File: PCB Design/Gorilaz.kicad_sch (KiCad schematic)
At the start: 57 parts, among them J1 Conn_01x13, J2 Conn_01x13, J3 Conn_01x13, J4 Conn_01x13, J5 HRO_TYPE-C-31-M-14, J5 Thermistor, J6 Battery, J6 Thermistor, J7 Conn_01x13, J8 Conn_01x13, J9 Battery, J9 TC2030_SWD, Q2 2N7002, SW1 PWR, SW4 RST, U1 SRV05-4, U10 MAX17048, U3 BQ24075, U4 DW01A, U5 FS8205, U8 nRF52840_moko_mk08

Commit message: LED package
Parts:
- D1, D2, D3, D4: footprint LED_THT:LED_D3.0mm -> LED_SMD:LED_1206_3216Metric
- R1, R2, R3, R4: value R_US -> 10k; footprint Resistor_THT:R_Axial_DIN0204_L3.6mm_D1.6mm_P5.08mm_Horizontal -> Resistor_SMD:R_0805_2012Metric

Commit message: schema update
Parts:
- removed D4: LED_ALT, LED_SMD:LED_1206_3216Metric, symbol kicad_port-rescue:LED_ALT-Device
- removed J5, J6: Thermistor, Connector_JST:JST_PH_S2B-PH-K_1x02_P2.00mm_Horizontal, symbol Connector_Generic_MountingPin:Conn_01x02_MountingPin
- removed J9: Battery, PCM_marbastlib-various:Molex_Pico-EZmate_78171-0002_1x02-1MP_P1.20mm_Vertical, symbol Connector_Generic_MountingPin:Conn_01x02_MountingPin
- removed R14, R16: 5k, Resistor_SMD:R_0402_1005Metric, symbol Device:R_Small
- removed R4: 10k, Resistor_SMD:R_0805_2012Metric, symbol kicad_port-rescue:R_US-Device
- J1, J2, J7, J8: footprint kinesisMod_board_connectors:Molex_0039532135 -> Local:Molex_0039532135
- J3: footprint kinesisMod_board_connectors:Molex_039532134 -> Local:Molex_0039532135
- J4: footprint kinesisMod_board_connectors:Molex_039532134 -> Molex_0039532135
- J6: footprint PCM_marbastlib-various:Molex_Pico-EZmate_78171-0002_1x02-1MP_P1.20mm_Vertical -> Local:Molex_Pico-EZmate_78171-0002_1x02-1MP_P1.20mm_Vertical
- J9: footprint PCM_marbastlib-various:CON_TC2030_outlined -> Local:CON_TC2030_outlined
- SW1: footprint PCM_marbastlib-various:SW_MSK12C02-HB -> Mastarlib:SW_MSK12C02-HB
- SW4: footprint PCM_marbastlib-various:SW_SPST_SKQG_WithStem -> Button_Switch_SMD:SW_SPST_SKQG_WithStem
- U10: footprint Package_DFN_QFN:DFN-8-1EP_2x2mm_P0.5mm_EP0.7x1.3mm -> Local:DFN-8-1EP_2x2mm_P0.5mm_EP0.7x1.3mm
- U8: footprint PCM_marbastlib-various:nRF52840_moko_mk08 -> Mastarlib:nRF52840_moko_mk08
- renumbered R1 to R20, R2 to R21, R3 to R22, R6 to R4, R7 to R6
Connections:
- net UG_EN: no longer names the net of U8.49 (P1.00)
- net UG_LV: no longer names the net of U8.31 (P0.22)
- no-connect marks 31 -> 30
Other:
- note added: "LED2: Battery Charging"
- note removed: "Overtemperature protection (BQ24075) Use a 10k thermistor"
- note removed: "Overtemperature protection (TP4056) For values of R15/R16 as well as the thermistor, refer to the datasheet."
- moved on the sheet: C17, C6, C7, C8, J6, LED2, R10, R15, R17, R18, R19, R9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

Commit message: v0
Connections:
- net LED_CAPS_LOCK: now also U8.13 (P0.04-A); no longer U8.1 (P0.03-LF-A)
- net LED_KEYPAD: now also U8.16 (P0.08); no longer U8.4 (P0.29-LF-A)
- net LED_NUM_LOCK: now also U8.14 (P0.06); no longer U8.2 (P0.02-LF-A)
- net LED_SCROLL_LOCK: now also U8.15 (P0.11); no longer U8.3 (P0.28-LF-A)
- net col0: now also U8.33 (P0.24); no longer U8.21 (P0.12)
- net col1: now also U8.23 (P0.14); no longer U8.22 (P0.13)
- net col2: now also U8.22 (P0.13); no longer U8.23 (P0.14)
- net col3: now also U8.21 (P0.12); no longer U8.24 (P0.15)
- net col4: now also U8.18 (P0.10-LF-NFC); no longer U8.25 (P0.16)
- net col5: now also U8.1 (P0.03-LF-A); no longer U8.26 (P0.17)
- net col6: now also U8.17 (P0.09-LF-NFC); no longer U8.28 (P0.19)
- net row0: now also U8.24 (P0.15); no longer U8.35 (P1.10-LF)
- net row1: now also U8.25 (P0.16); no longer U8.36 (P1.11-LF)
- net row10: now also U8.2 (P0.02-LF-A); no longer U8.52 (P1.03-LF)
- net row11: now also U8.4 (P0.29-LF-A); no longer U8.53 (P1.04-LF)
- net row12: now also U8.34 (P0.25); no longer U8.54 (P1.05-LF)
- net row13: now also U8.32 (P0.23); no longer U8.55 (P1.06-LF)
- net row14: now also U8.31 (P0.22); no longer U8.56 (P1.07-LF)
- net row2: now also U8.26 (P0.17); no longer U8.37 (P1.12-LF)
- net row3: now also U8.28 (P0.19); no longer U8.38 (P1.13-LF)
- net row4: now also U8.29 (P0.20); no longer U8.40 (P1.14-LF)
- net row5: now also U8.30 (P0.21); no longer U8.41 (P1.15-LF)
- net row6: now also U8.40 (P1.14-LF); no longer U8.44 (P1.08)
- net row7: now also U8.5 (P0.30-LF-A); no longer U8.45 (P1.09)
- net row8: now also U8.6 (P0.31-LF-A); no longer U8.50 (P1.01-LF)
- net row9: now also U8.3 (P0.28-LF-A); no longer U8.51 (P1.02-LF)
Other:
- note added: "Battery management"
- note added: "Optional debug port"
- note added: "Voltage sensing"
- note removed: "Battery Management (Additional considerations)"
- note removed: "Battery management (advanced)"
- note removed: "Voltage sensing (advanced)"
- moved on the sheet: C17, C8, D1, D2, D3, J6, Q2, R15, R17, R18, R19, R20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

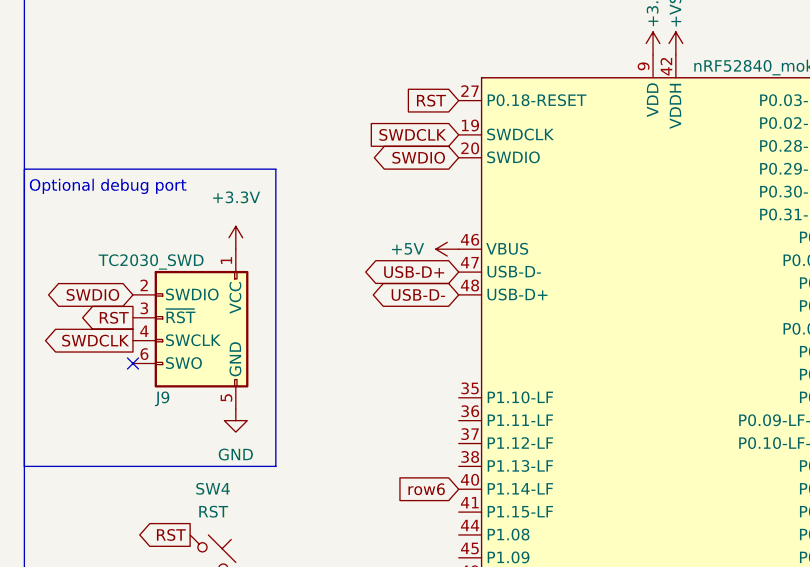
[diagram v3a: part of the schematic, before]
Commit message: Data lane correction
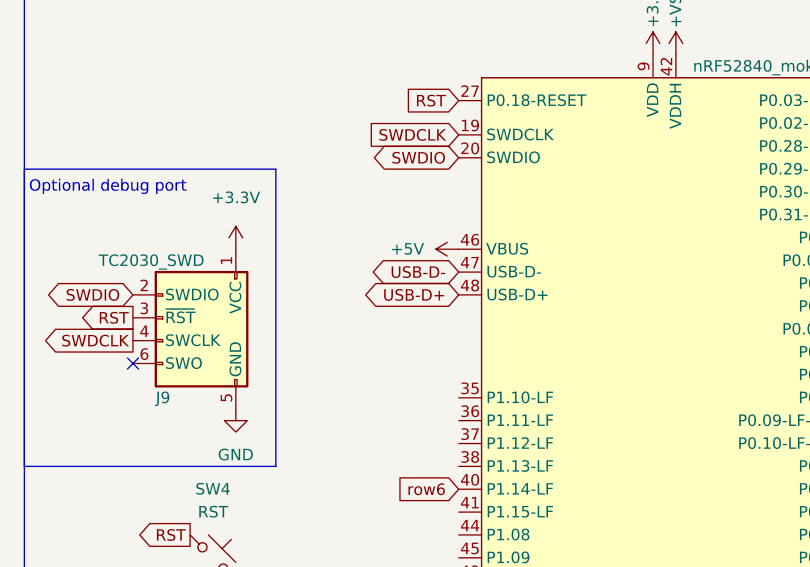
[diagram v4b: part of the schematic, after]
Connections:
- net USB-D+: now also U8.48 (USB-D+); no longer U8.47 (USB-D-)
- net USB-D-: now also U8.47 (USB-D-); no longer U8.48 (USB-D+)
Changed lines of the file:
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@@
+		)
+	)
+	(global_label "USB-D-"
+		(shape bidirectional)
+		(at 107.95 144.78 180)
+		(fields_autoplaced yes)
+		(effects
+			(font
+				(size 1.27 1.27)
+			)
+			(justify right)
+		)
+		(property "Intersheetrefs" "${INTERSHEET_REFS}"
+			(at 97.3121 144.8594 0)
+			(effects
+				(font
+					(size 1.27 1.27)
+				)
+				(justify right)
+				(hide yes)
+			)
 		)
 	)
@@
 		)
 	)
-	(global_label "USB-D+"
-		(shape bidirectional)
-		(at 107.95 144.78 180)
-		(fields_autoplaced yes)
-		(effects
-			(font
-				(size 1.27 1.27)
-			)
-			(justify right)
-		)
-		(property "Intersheetrefs" "${INTERSHEET_REFS}"
-			(at 97.3121 144.8594 0)
-			(effects
-				(font
-					(size 1.27 1.27)
-				)
-				(justify right)
-				(hide yes)
-			)
-		)
-	)
 	(global_label "col6"
 		(shape input)
@@
 		)
 	)
-	(global_label "USB-D-"
-		(shape bidirectional)
-		(at 107.95 147.32 180)
-		(fields_autoplaced yes)
-		(effects
-			(font
-				(size 1.27 1.27)
-			)
-			(justify right)
-		)
-		(property "Intersheetrefs" "${INTERSHEET_REFS}"
-			(at 97.3121 147.3994 0)
-			(effects
-				(font
-					(size 1.27 1.27)
-				)
-				(justify right)
-				(hide yes)
-			)
-		)
-	)
 	(global_label "row6"
 		(shape input)
@@
 				(hide yes)
 			)
+		)
+	)
+	(global_label "USB-D+"
+		(shape bidirectional)
+		(at 107.95 147.32 180)
+		(fields_autoplaced yes)
+		(effects
+			(font
+				(size 1.27 1.27)
+			)
+			(justify right)
+		)
+		(property "Intersheetrefs" "${INTERSHEET_REFS}"
+			(at 97.3121 147.3994 0)
+			(effects
+				(font
+					(size 1.27 1.27)
+				)
+				(justify right)
+				(hide yes)
+			)

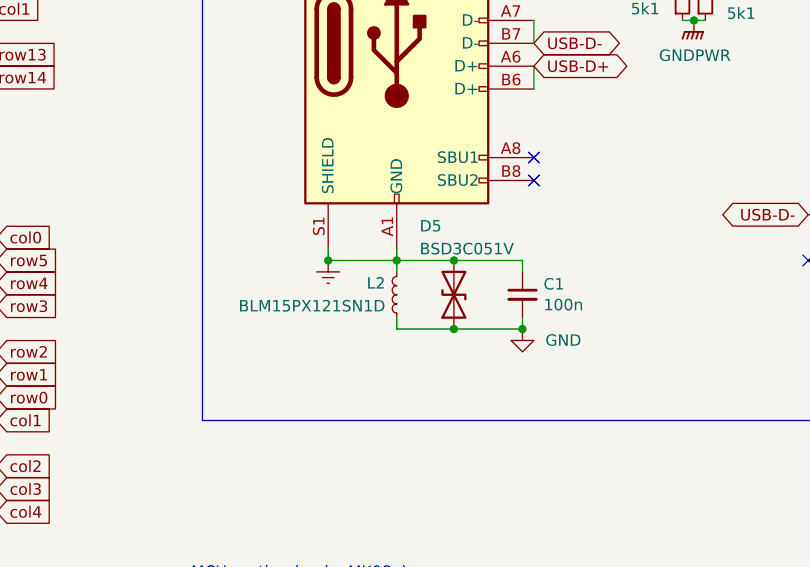
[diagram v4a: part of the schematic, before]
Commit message: USB-C update
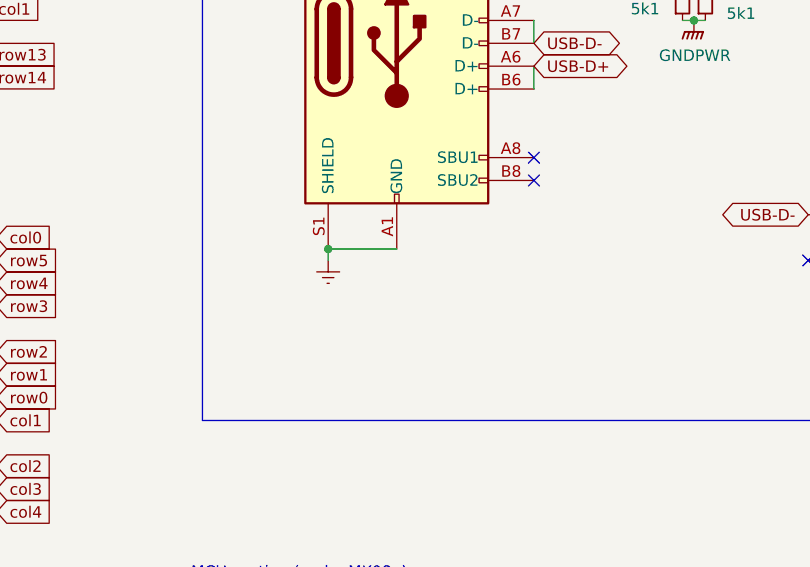
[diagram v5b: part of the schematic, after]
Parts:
- removed C1: 100n, Capacitor_SMD:C_0402_1005Metric, symbol Device:C_Small
- removed D5: BSD3C051V, Diode_SMD:D_SOD-323, symbol Device:D_TVS
- removed L2: BLM15PX121SN1D, Inductor_SMD:L_0402_1005Metric, symbol Device:L_Small
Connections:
- net Earth is gone; now on net GND: J5.A1 (GND), J5.A12 (GND), J5.B1 (GND), J5.B12 (GND), J5.S1 (SHIELD)

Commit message: power managemnt rework
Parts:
- removed J9: TC2030_SWD, Local:CON_TC2030_outlined, symbol PCM_marbastlib-various:TC2030_SWD
- removed Q2: 2N7002, Package_TO_SOT_SMD:SOT-23, symbol Transistor_FET:2N7002
- removed R6: 10k, Resistor_SMD:R_0402_1005Metric, symbol Device:R_Small
- removed R7: 100R, Resistor_SMD:R_0402_1005Metric, symbol Device:R_Small
- removed R8: 100k, Resistor_SMD:R_0402_1005Metric, symbol Device:R_Small
- removed SW1: PWR, Mastarlib:SW_MSK12C02-HB, symbol Switch:SW_Push_SPDT
- added LED1: pwr ON, LED_SMD:LED_0402_1005Metric, symbol Device:LED_Small
- added R1: 1k, Resistor_SMD:R_0402_1005Metric, symbol Device:R_Small
- added R2: 5k1, Resistor_SMD:R_0402_1005Metric, symbol Device:R_Small
- added SW1: SW_DPST_x2, symbol Switch:SW_DPST_x2
- LED2: value orange -> Charing
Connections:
- net GNDPWR is gone; now on net GND: R4.1, R5.1
- net SYSOFF is gone; now on net GND: U3.15 (SYSOFF)
- net +3.3V: now also R2.2
- net +BATT: now also SW1.2 (B); no longer J6.1 (Pin_1)
- net +VSW: now also R1.2
- net ALERT: now also R2.1
- net GND: now also LED1.1 (K)
- net LED_NUM_LOCK: no longer R21.2
- net LED_CAPS_LOCK renamed LED_POWER_ON
- net LED_KEYPAD renamed LED_BATT_WARN
- net LED_BATT_WARN: now also R22.2
- net LED_SCROLL_LOCK renamed LED_BLE
- net LED_BLE: now also R21.2; no longer R22.2
- new net: LED1.2 (A), R1.1
- new net: J6.1 (Pin_1), SW1.1 (A)
- no-connect marks 30 -> 45
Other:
- note added: "Battery Charging"
- note added: "Battery Protection"
- note added: "OTHER"
- note removed: "LED2: Battery Charging"
- note removed: "Optional debug port"
- note removed: "SYSOFF 1 (SW1 pos 1): Batt OFF SYSOFF 0 (SW1 pos 3): Batt ON"
- note removed: "TMR: (10 x 48 s/kOhm) * 47 kOhm = 22560s = 6.27h ILIM: 1550 AOhm / 1500 Ohm = 1.03 A = 1030 mA ISET: 890 AOhm / 3900 Ohm = 0.228 A = 230 mA EN1: 1, EN2: 0 = 475 mA MAX TS: 10 kOhm to GND = no OTP"
- moved on the sheet: C17, C5, C6, C7, C8, D1, D2, D3, F1, J5, J6, L1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

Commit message: big updates push
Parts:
- removed C7: 4u7, Capacitor_SMD:C_0402_1005Metric, symbol Device:C_Small
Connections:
- net LED_BATT_WARN: now also U8.15 (P0.11); no longer U8.16 (P0.08)
- net LED_BLE: now also U8.14 (P0.06); no longer U8.15 (P0.11)
- net LED_NUM_LOCK: now also U8.16 (P0.08); no longer U8.14 (P0.06)
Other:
- moved on the sheet: R2
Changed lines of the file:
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@@
 	)
 	(junction
-		(at 267.97 99.06)
-		(diameter 0.9144)
-		(color 0 0 0 0)
-	)
-	(junction
 		(at 132.08 201.93)
 		(diameter 0)
@@
 	(wire
 		(pts
-			(xy 293.37 41.91) (xy 298.45 41.91)
-		)
-		(stroke
-			(width 0)
-			(type default)
-		)
-	)
-	(wire
-		(pts
 			(xy 30.48 146.05) (xy 31.115 146.05)
 		)
@@
 	(wire
 		(pts
-			(xy 288.29 41.91) (xy 293.37 41.91)
-		)
-		(stroke
-			(width 0)
-			(type default)
-		)
-	)
-	(wire
-		(pts
 			(xy 390.525 39.37) (xy 391.16 39.37)
 		)
@@
 	(wire
 		(pts
+			(xy 293.37 41.91) (xy 298.45 41.91)
+		)
+		(stroke
+			(width 0)
+			(type default)
+		)
+	)
+	(wire
+		(pts
 			(xy 86.36 55.88) (xy 102.87 55.88)
 		)
@@
 	(wire
 		(pts
+			(xy 288.29 41.91) (xy 288.29 43.18)
+		)
+		(stroke
+			(width 0)
+			(type default)
+		)
+	)
+	(wire
+		(pts
 			(xy 31.75 50.8) (xy 32.385 50.8)
 		)
@@
 	(wire
 		(pts
-			(xy 288.29 46.99) (xy 288.29 53.34)
+			(xy 288.29 48.26) (xy 288.29 53.34)
 		)
 		(stroke
@@
 	(wire
 		(pts
+			(xy 288.29 41.91) (xy 293.37 41.91)
+		)
+		(stroke
+			(width 0)
+			(type default)
+		)
+	)
+	(wire
+		(pts
 			(xy 32.385 45.72) (xy 36.83 45.72)
 		)
@@
 		)
 	)
+	(global_label "LED_BATT_WARN"
+		(shape input)
+		(at 153.67 156.21 0)
+		(fields_autoplaced yes)
+		(effects
+			(font
+				(size 1.27 1.27)
+			)
+			(justify left)
+		)
+		(property "Intersheetrefs" "${INTERSHEET_REFS}"
+			(at 171.4718 156.21 0)
+			(effects
+				(font
+					(size 1.27 1.27)
+				)
+				(justify left)
+				(hide yes)
+			)
+		)
+	)
 	(global_label "col6"
 		(shape input)
@@
 		)
 	)
+	(global_label "LED_BLE"
+		(shape input)
+		(at 153.67 153.67 0)
+		(fields_autoplaced yes)
+		(effects
+			(font
+				(size 1.27 1.27)
+			)
+			(justify left)
+		)
+		(property "Intersheetrefs" "${INTERSHEET_REFS}"
+			(at 164.517 153.67 0)
+			(effects
+				(font
+					(size 1.27 1.27)
+				)
+				(justify left)
+				(hide yes)
+			)
+		)
+	)
 	(global_label "LED_BATT_WARN"
 		(shape input)
@@
 		)
 	)
-	(global_label "LED_BATT_WARN"
-		(shape input)
-		(at 153.67 158.75 0)
-		(fields_autoplaced yes)
-		(effects
-			(font
-				(size 1.27 1.27)
-			)
-			(justify left)
-		)
-		(property "Intersheetrefs" "${INTERSHEET_REFS}"
-			(at 171.4718 158.75 0)
-			(effects
-				(font
-					(size 1.27 1.27)
-				)
-				(justify left)
-				(hide yes)
-			)
-		)
-	)
 	(global_label "row4"
 		(shape input)
@@
 		)
 	)
-	(global_label "LED_BLE"
-		(shape input)
-		(at 153.67 156.21 0)
-		(fields_autoplaced yes)
-		(effects
-			(font
-				(size 1.27 1.27)
-			)
-			(justify left)
-		)
-		(property "Intersheetrefs" "${INTERSHEET_REFS}"
-			(at 164.517 156.21 0)
-			(effects
-				(font
-					(size 1.27 1.27)
-				)
-				(justify left)
-				(hide yes)
-			)
-		)
-	)
 	(global_label "col0"
 		(shape input)
@@
 		)
 	)
-	(global_label "LED_NUM_LOCK"
-		(shape input)
-		(at 153.67 153.67 0)
-		(fields_autoplaced yes)
-		(effects
-			(font
-				(size 1.27 1.27)
-			)
-			(justify left)
-		)
-		(property "Intersheetrefs" "${INTERSHEET_REFS}"
-			(at 171.0485 153.67 0)
-			(effects
-				(font
-					(size 1.27 1.27)
-				)
-				(justify left)
-				(hide yes)
-			)
-		)
-	)
 	(global_label "col6"
 		(shape input)
@@
 		)
 	)
+	(global_label "LED_NUM_LOCK"
+		(shape input)
+		(at 153.67 158.75 0)
+		(fields_autoplaced yes)
+		(effects
+			(font
+				(size 1.27 1.27)
+			)
+			(justify left)
+		)
+		(property "Intersheetrefs" "${INTERSHEET_REFS}"
+			(at 171.0485 158.75 0)
+			(effects
+				(font
+					(size 1.27 1.27)
+				)
+				(justify left)
+				(hide yes)
+			)
+		)
+	)
 	(global_label "LED_POWER_ON"
 		(shape input)
@@
 	)
 	(symbol
-		(lib_id "Device:C_Small")
-		(at 267.97 101.6 0)
-		(unit 1)
-		(exclude_from_sim no)
-		(in_bom yes)
-		(on_board yes)
-		(dnp no)
-		(property "Reference" "C7"
-			(at 270.764 101.0666 0)
-			(effects
-				(font
-					(size 1.27 1.27)
-				)
-				(justify left)
-			)
-		)
-		(property "Value" "4u7"
-			(at 270.764 103.378 0)
-			(effects
-				(font
-					(size 1.27 1.27)
-				)
-				(justify left)
-			)
-		)
-		(property "Footprint" "Capacitor_SMD:C_0402_1005Metric"
-			(at 267.97 101.6 0)
-			(effects
-				(font
-					(size 1.27 1.27)
-				)
-				(hide yes)
-			)
-		)
-		(property "Datasheet" "~"
-			(at 267.97 101.6 0)
-			(effects
-				(font
-					(size 1.27 1.27)
-				)
-				(hide yes)
-			)
-		)
-		(property "Description" ""
-			(at 267.97 101.6 0)
-			(effects
-				(font
-					(size 1.27 1.27)
-				)
-				(hide yes)
-			)
-		)
-		(property "LCSC" ""
-			(at 267.97 101.6 0)
-			(effects
-				(font
-					(size 1.27 1.27)
-				)
-				(hide yes)
-			)
-		)
-		(property "Notes" "X7R, 10%"
-			(at 267.97 101.6 0)
-			(effects
-				(font
-					(size 1.27 1.27)
-				)
-				(hide yes)
-			)
-		)
-		(pin "1"
-		)
-		(pin "2"
-		)
-		(instances
-			(project "Gorilaz"
-				(path "/46ef0abf-42df-44ff-8272-0b82956755c4"
-					(reference "C7")
-					(unit 1)
-				)
-			)
-		)
-	)
-	(symbol
 		(lib_id "Connector:USB_C_Receptacle_USB2.0")
 		(at 71.12 63.5 0)
@@
 	(symbol
 		(lib_id "Device:R_Small")
-		(at 288.29 44.45 180)
+		(at 288.29 45.72 180)
 		(unit 1)
 		(exclude_from_sim no)
@@
 		(dnp no)
 		(property "Reference" "R2"
-			(at 285.75 43.18 0)
+			(at 285.75 44.45 0)
 			(effects
 				(font
@@
 		)
 		(property "Value" "5k1"
-			(at 285.75 45.72 0)
+			(at 285.75 46.99 0)
 			(effects
 				(font
@@
 		)
 		(property "Footprint" "Resistor_SMD:R_0402_1005Metric"
-			(at 288.29 44.45 0)
+			(at 288.29 45.72 0)
 			(effects
 				(font
@@
 		)
 		(property "Datasheet" "~"
-			(at 288.29 44.45 0)
+			(at 288.29 45.72 0)
 			(effects
 				(font
@@
 		)
 		(property "Description" ""
-			(at 288.29 44.45 0)
+			(at 288.29 45.72 0)
 			(effects
 				(font

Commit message: render update
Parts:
- renumbered J2 to J1, J4 to J2, J8 to J3, J1 to J4, J3 to J5, J7 to J6, J6 to J7, J5 to J8
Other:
- note added: "Left Side"
- note added: "Right Side"
- moved on the sheet: C17, C5, C6, C8, D1, D2, D3, F1, J1, J2, J3, J4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
